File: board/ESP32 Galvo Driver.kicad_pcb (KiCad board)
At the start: 2 copper layers, 200 x 50 mm, 78 parts, among them J1 15V Power In, J10 15V Supply In, J11 AudioJack3_SwitchTR, J12 LASER_EN, J13 FAN, J2 RED, J3 GREEN, J4 BLUE, J5 Native USB, J6 Galvo X Output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

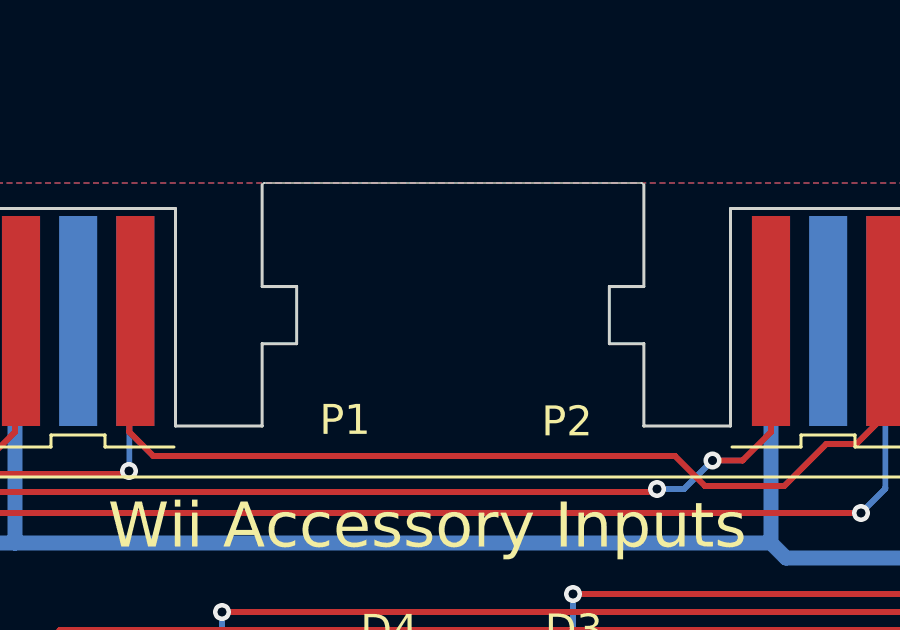
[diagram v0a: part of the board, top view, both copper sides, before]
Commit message: ILDA test pattern WIP
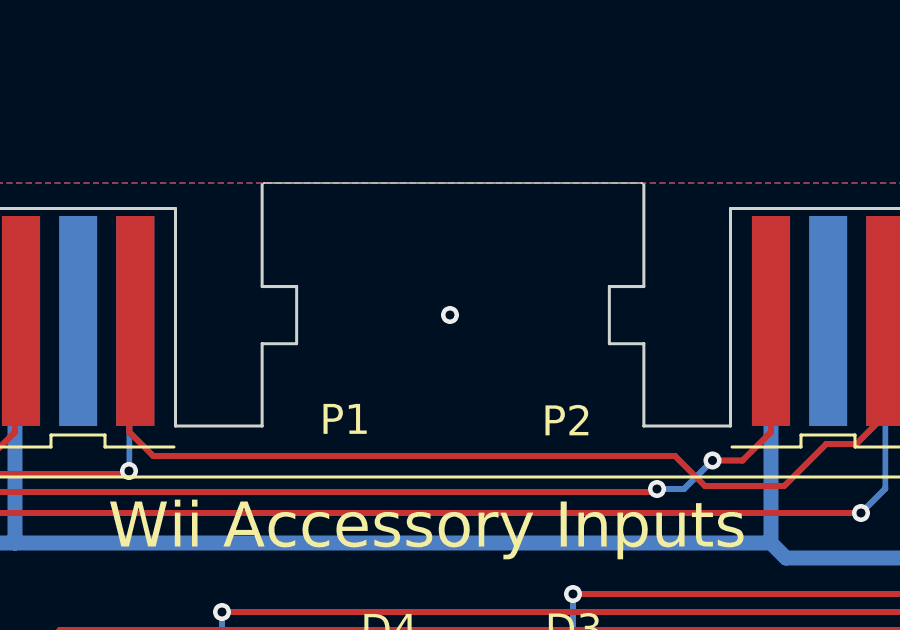
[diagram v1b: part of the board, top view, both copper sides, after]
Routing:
- net GND: vias 19 -> 20
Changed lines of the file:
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@@
+	)
+	(via
+		(at 139.3 59.4)
+		(size 0.6)
+		(drill 0.3)
+		(layers "F.Cu" "B.Cu")
+		(free yes)
+		(net 2)
 	)
 	(via

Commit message: update board
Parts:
- added G***: LOGO, SparkFun-Qwiic:qwiic_5.5mm, F.Cu at (143.1, 58.5)
- added G***: LOGO, SparkFun-Qwiic:qwiic_5.5mm, F.Cu at (168.2, 58.5)
- added J14: Laser Key, Connector_JST:JST_XH_B2B-XH-A_1x02_P2.50mm_Vertical, F.Cu at (140.3, 93.8)
- added J15: Conn_01x05, Connector_PinHeader_2.54mm:PinHeader_1x05_P2.54mm_Vertical, F.Cu at (62.0, 64.2)
- added J16: Quiic 1, Connector_JST:JST_SH_BM04B-SRSS-TB_1x04-1MP_P1.00mm_Vertical, F.Cu at (139.5, 59.7)
- added J17: Quiic 2, Connector_JST:JST_SH_BM04B-SRSS-TB_1x04-1MP_P1.00mm_Vertical, F.Cu at (164.6, 59.7)
- added JP1: DAC X Select, Jumper:SolderJumper-3_P1.3mm_Bridged12_RoundedPad1.0x1.5mm, B.Cu at (116.7, 73.0)
- added JP2: DAC Y Select, Jumper:SolderJumper-3_P1.3mm_Bridged12_RoundedPad1.0x1.5mm, B.Cu at (116.7, 78.0)
- added JP3: Key Bypass, Jumper:SolderJumper-2_P1.3mm_Open_TrianglePad1.0x1.5mm, B.Cu at (141.7, 90.5)
- added R30: 100k, Resistor_SMD:R_0603_1608Metric_Pad0.98x0.95mm_HandSolder, F.Cu at (100.2, 92.3)
- added R31: 27k, Resistor_SMD:R_0603_1608Metric_Pad0.98x0.95mm_HandSolder, F.Cu at (96.9, 92.3)
- added U5: MCP4922-ESL, Package_SO:SOIC-14_3.9x8.7mm_P1.27mm, F.Cu at (95.0, 83.3)
- P1: value CONN_WII -> Wii 1
- P2: value CONN_WII -> Wii 2
- moved R24 0.65 mm to (103.5, 92.2)
- turned Q3 to 180 degrees
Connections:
- Q3 pad 2: +12V -> Net-(J14-Pin_1)
- R24 pad 2: +12V -> Net-(J14-Pin_1)
- U1 pad 10: /DAC_X -> /DAC_X_INT
- U1 pad 11: /DAC_Y -> /DAC_Y_INT
- U1 pad 17: unconnected-(U1-GPIO9/TOUCH9/ADC1_CH8/FSPIHD-Pad17) -> /KEY_SENSE
- U1 pad 25: unconnected-(U1-SPIIO5/GPIO34/FSPICS0-Pad25) -> /SPI_CS_DAC
- U1 pad 28: unconnected-(U1-SPIIO6/GPIO35/FSPID-Pad28) -> /SPI_MOSI
- U1 pad 29: unconnected-(U1-SPIIO7/GPIO36/FSPICLK-Pad29) -> /SPI_SCK
- U1 pad 30: unconnected-(U1-SPIDQS/GPIO37/FSPIQ-Pad30) -> /SPI_MISO
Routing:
- net /DAC_X_INT: track 0.00 -> 51.7 mm, vias 0 -> 1
- net Net-(J14-Pin_1): track 0.00 -> 49.3 mm
- net +3.3V: track 211.7 -> 257.1 mm, vias 4 -> 7
- net /DAC_Y_INT: track 0.00 -> 45.2 mm, vias 0 -> 1
- net +12V: track 146.5 -> 101.5 mm, vias 2 -> 1
- net /DAC_X: track 58.2 -> 16.4 mm, vias 2 -> 1
- net /DAC_Y: track 77.2 -> 40.5 mm, vias 2 -> 1
- net GND: track 85.8 -> 55.2 mm
- net /I2C1_SDA: track 99.4 -> 125.1 mm, vias 3 -> 4
- net /I2C1_SCL: track 87.8 -> 110.8 mm, vias 4 -> 2
- net /I2C0_SCL: track 75.3 -> 98.2 mm
- net /DAC_X_EXT: track 0.00 -> 22.0 mm, vias 0 -> 1
- net /DAC_Y_EXT: track 0.00 -> 21.4 mm, vias 0 -> 1
- net /KEY_SENSE: track 0.00 -> 20.6 mm, vias 0 -> 2
- net /I2C0_SDA: track 82.3 -> 102.3 mm, vias 1 -> 2
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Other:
- board text added: "DAC Selection"
- board text added: "DTR"
- board text added: "ESP32"
- board text added: "GND"
- board text added: "Key Bypass"
- board text added: "Laser Key"
- board text added: "MCP4922"
- board text added: "RTS"
- board text added: "RX"
- board text added: "TX"
- board text added: "X"
- board text added: "Y"

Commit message: gtfs, litt.chr parsing
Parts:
- removed the REF** at (229.2, 62.8)
- removed the REF** at (251.8, 80.0)
- added C10: 10uF, Capacitor_SMD:C_0603_1608Metric_Pad1.08x0.95mm_HandSolder, F.Cu at (91.7, 92.8)
- added C11: 0.1uF, Capacitor_SMD:C_0603_1608Metric_Pad1.08x0.95mm_HandSolder, F.Cu at (91.7, 90.3)
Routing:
- net GND: track 55.2 -> 78.7 mm, vias 20 -> 22
- net +3.3V: track 257.1 -> 266.8 mm
- net /I2C0_SDA: track 102.3 -> 99.1 mm
- net /SPI_CS_DAC: track 11.4 -> 10.4 mm
- net /SPI_SCK: track 14.9 -> 14.0 mm
- net /SPI_MOSI: track 15.6 -> 14.9 mm
- net Net-(J12-Pin_2): track 8.96 -> 8.34 mm
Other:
- board text added: "Avoid Exposure to Beam"
- board text added: "Caution!"
- board text added: "Class 3B Laser - 200mW"
- board text added: "Line Voltage Present"
- board text added: "System Diagram"

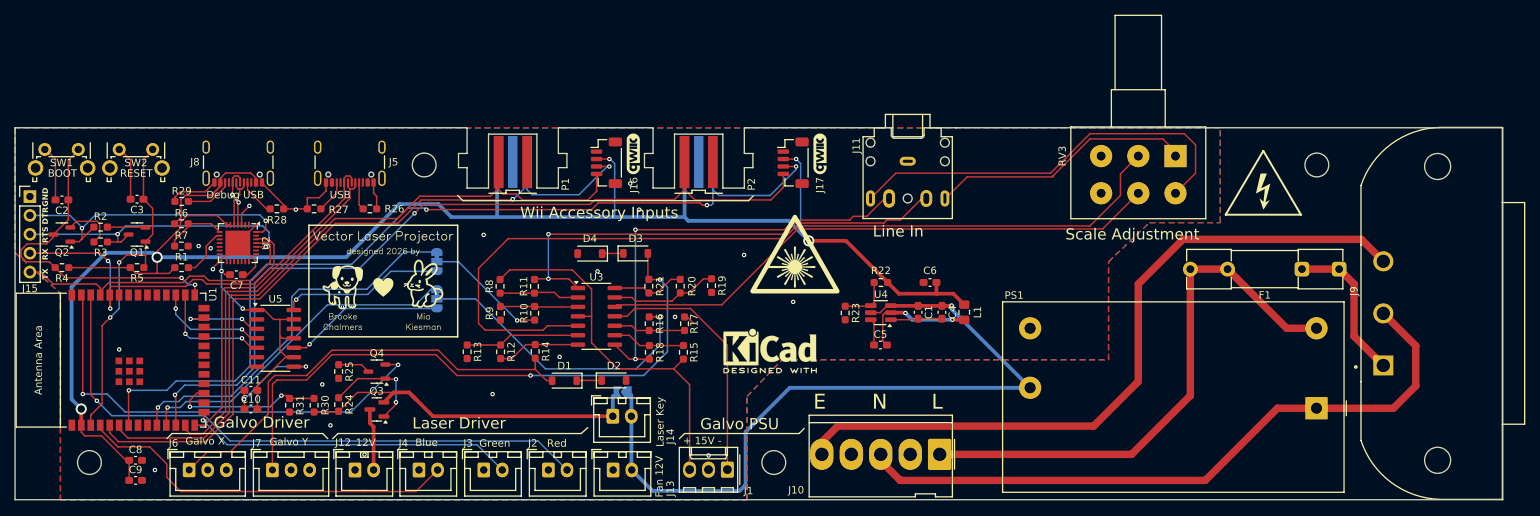
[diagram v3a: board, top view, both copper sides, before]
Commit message: switch to pinouts from PCB, separate package for vector text
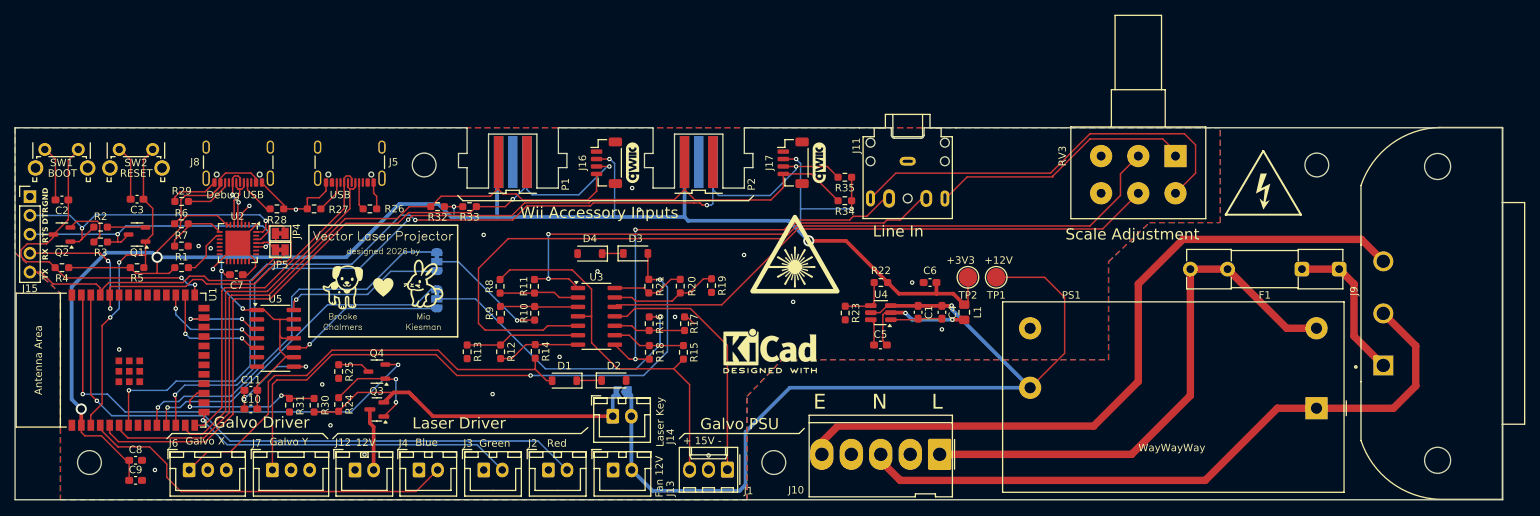
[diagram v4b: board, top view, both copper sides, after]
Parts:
- added JP4: UART_RX, Jumper:SolderJumper-2_P1.3mm_Bridged_Pad1.0x1.5mm, F.Cu at (95.7, 69.2)
- added JP5: UART_TX, Jumper:SolderJumper-2_P1.3mm_Bridged_Pad1.0x1.5mm, F.Cu at (95.7, 71.4)
- added R32: 10k, Resistor_SMD:R_0603_1608Metric_Pad0.98x0.95mm_HandSolder, F.Cu at (116.8, 65.6)
- added R33: 10k, Resistor_SMD:R_0603_1608Metric_Pad0.98x0.95mm_HandSolder, F.Cu at (121.1, 65.6)
- added R34: 10k, Resistor_SMD:R_0603_1608Metric_Pad0.98x0.95mm_HandSolder, F.Cu at (171.6, 64.8)
- added R35: 10k, Resistor_SMD:R_0603_1608Metric_Pad0.98x0.95mm_HandSolder, F.Cu at (171.6, 61.6)
- added TP1: 12V, TestPoint:TestPoint_Pad_D2.5mm, F.Cu at (191.9, 75.1)
- added TP2: 3.3V, TestPoint:TestPoint_Pad_D2.5mm, F.Cu at (188.1, 75.1)
- moved G*** 1.20 mm to (143.0, 59.7)
- moved G*** 1.20 mm to (168.1, 59.7)
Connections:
- U2 pad 25: /UART_TX -> Net-(JP5-A)
- U2 pad 26: /UART_RX -> Net-(JP4-A)
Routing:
- net +12V: track 101.4 -> 125.8 mm
- net +3.3V: track 266.8 -> 285.2 mm, vias 7 -> 9
- net /I2C1_SCL: track 110.8 -> 119.6 mm
- net /I2C1_SDA: track 125.1 -> 131.7 mm
- net Net-(JP4-A): track 0.00 -> 5.31 mm
- net Net-(JP5-A): track 0.00 -> 3.06 mm
- net /UART_RX: track 49.5 -> 51.9 mm
- net /UART_TX: track 40.6 -> 38.7 mm
- net /USB_DM: track 48.6 -> 49.4 mm
- net /USB_DP: track 46.1 -> 46.9 mm
- net GND: track 78.7 -> 78.6 mm, vias 22 -> 24
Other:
- board text added: "+12V"
- board text added: "+3V3"
- board text added: "WayWayWay"

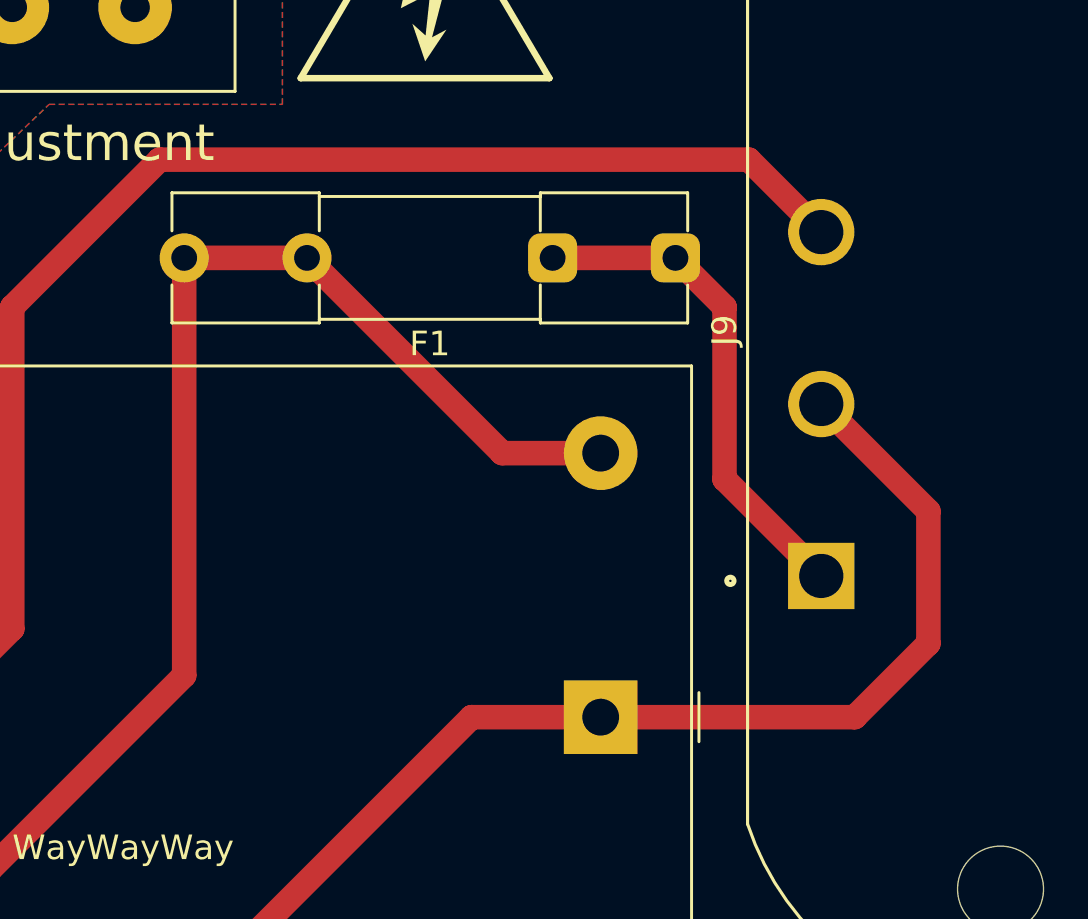
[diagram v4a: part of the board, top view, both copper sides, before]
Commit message: board updates: fix improper wiring of AC input
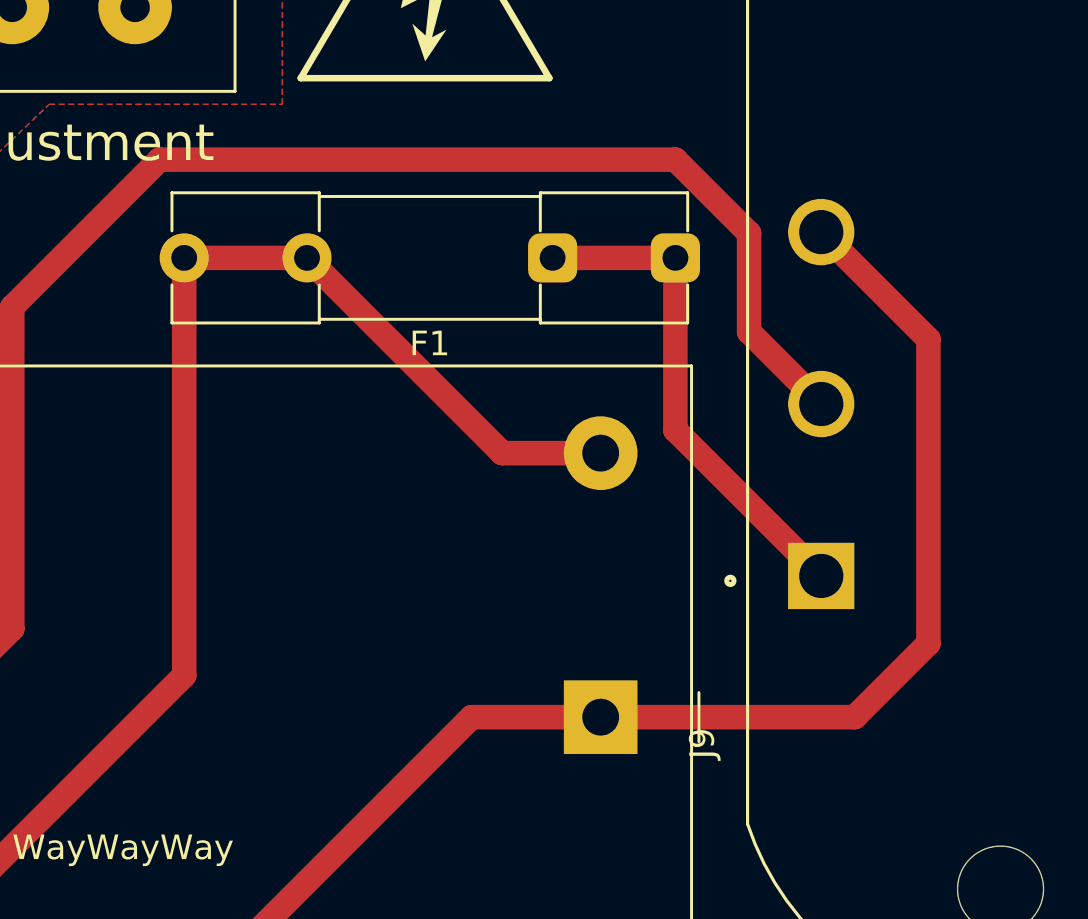
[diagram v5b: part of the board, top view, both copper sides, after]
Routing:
- net /AC_N: track 89.8 -> 96.8 mm
- net /EARTH: track 97.3 -> 102.6 mm
